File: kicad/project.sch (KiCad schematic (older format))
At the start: 33 parts, among them J1 Conn_01x05, J2 Conn_01x01, SW1 SW_DPDT_x2, U1 STM32L031F4Px

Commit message: Switches
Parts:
- removed SW1: SW_DPDT_x2, Buttons_Switches_THT:SW_Micro_SPST, symbol SW_DPDT_x2
- added R8: 1k, Resistors_SMD:R_0603_HandSoldering, symbol R
- added SW1: SW_SPDT, theapi:SW_Micro_SPST, symbol SW_SPDT
- added SW2: SW_SPDT, Buttons_Switches_THT:SW_Micro_SPST, symbol SW_SPDT
- added SW3: SW_Push, Buttons_Switches_THT:SW_PUSH_6mm, symbol SW_Push
- J2: footprint Mounting_Holes:MountingHole_2.5mm -> Mounting_Holes:MountingHole_2.5mm_Pad
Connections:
- net GND: now also R8.1
- net at U1.10 (PA4): now also SW3.1
- net +BATT renamed BATT_SW
- net BATT_SW: now also SW1.1 (A), SW2.1 (A)
- net BATT_UNSWITCHED renamed BATT+
- net BATT+: now also SW1.2 (B), SW2.2 (B)
- new net: R8.2, SW3.2
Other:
- note added: "Different sized switch\nfootprint options"
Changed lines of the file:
@@
 SWDIO
 $Comp
-L +BATT #PWR03
-U 1 1 5A9FF0BE
-P 5625 2325
-F 0 "#PWR03" H 5625 2175 50  0001 C CNN
-F 1 "+BATT" H 5625 2465 50  0000 C CNN
-F 2 "" H 5625 2325 50  0001 C CNN
-F 3 "" H 5625 2325 50  0001 C CNN
-	1    5625 2325
-	1    0    0    -1
-$EndComp
-$Comp
-L +BATT #PWR04
-U 1 1 5A9FF0BF
-P 2525 2825
-F 0 "#PWR04" H 2525 2675 50  0001 C CNN
-F 1 "+BATT" H 2525 2965 50  0000 C CNN
-F 2 "" H 2525 2825 50  0001 C CNN
-F 3 "" H 2525 2825 50  0001 C CNN
-	1    2525 2825
-	1    0    0    -1
-$EndComp
-$Comp
-L GND #PWR05
+L GND #PWR04
 U 1 1 5A9FF0C0
 P 2525 3750
-F 0 "#PWR05" H 2525 3500 50  0001 C CNN
+F 0 "#PWR04" H 2525 3500 50  0001 C CNN
 F 1 "GND" H 2525 3600 50  0000 C CNN
 F 2 "" H 2525 3750 50  0001 C CNN
@@
 $EndComp
 $Comp
-L +BATT #PWR06
-U 1 1 5A9FF0C2
-P 3025 975
-F 0 "#PWR06" H 3025 825 50  0001 C CNN
-F 1 "+BATT" H 3025 1115 50  0000 C CNN
-F 2 "" H 3025 975 50  0001 C CNN
-F 3 "" H 3025 975 50  0001 C CNN
-	1    3025 975
-	1    0    0    -1
-$EndComp
-$Comp
-L GND #PWR07
+L GND #PWR05
 U 1 1 5A9FF0C3
 P 1250 2000
-F 0 "#PWR07" H 1250 1750 50  0001 C CNN
+F 0 "#PWR05" H 1250 1750 50  0001 C CNN
 F 1 "GND" H 1250 1850 50  0000 C CNN
 F 2 "" H 1250 2000 50  0001 C CNN
@@
 $EndComp
 $Comp
-L GND #PWR08
+L GND #PWR06
 U 1 1 5A9FF0C6
 P 5050 2600
-F 0 "#PWR08" H 5050 2350 50  0001 C CNN
+F 0 "#PWR06" H 5050 2350 50  0001 C CNN
 F 1 "GND" H 5050 2450 50  0000 C CNN
 F 2 "" H 5050 2600 50  0001 C CNN
@@
 $EndComp
 $Comp
-L GND #PWR09
+L GND #PWR07
 U 1 1 5A9FF0C7
 P 6300 2600
-F 0 "#PWR09" H 6300 2350 50  0001 C CNN
+F 0 "#PWR07" H 6300 2350 50  0001 C CNN
 F 1 "GND" H 6300 2450 50  0000 C CNN
 F 2 "" H 6300 2600 50  0001 C CNN
@@
 $EndComp
 $Comp
-L GND #PWR010
+L GND #PWR08
 U 1 1 5A9FF286
 P 10275 2475
-F 0 "#PWR010" H 10275 2225 50  0001 C CNN
+F 0 "#PWR08" H 10275 2225 50  0001 C CNN
 F 1 "GND" H 10275 2325 50  0000 C CNN
 F 2 "" H 10275 2475 50  0001 C CNN
@@
 $EndComp
 $Comp
-L GND #PWR011
+L GND #PWR09
 U 1 1 5A9FF752
 P 10275 2850
-F 0 "#PWR011" H 10275 2600 50  0001 C CNN
+F 0 "#PWR09" H 10275 2600 50  0001 C CNN
 F 1 "GND" H 10275 2700 50  0000 C CNN
 F 2 "" H 10275 2850 50  0001 C CNN
@@
 $EndComp
 $Comp
-L GND #PWR012
+L GND #PWR010
 U 1 1 5A9FF7FA
 P 10275 3250
-F 0 "#PWR012" H 10275 3000 50  0001 C CNN
+F 0 "#PWR010" H 10275 3000 50  0001 C CNN
 F 1 "GND" H 10275 3100 50  0000 C CNN
 F 2 "" H 10275 3250 50  0001 C CNN
@@
 $EndComp
 $Comp
-L GND #PWR013
+L GND #PWR011
 U 1 1 5A9FF80C
 P 10275 3625
-F 0 "#PWR013" H 10275 3375 50  0001 C CNN
+F 0 "#PWR011" H 10275 3375 50  0001 C CNN
 F 1 "GND" H 10275 3475 50  0000 C CNN
 F 2 "" H 10275 3625 50  0001 C CNN
@@
 $EndComp
 $Comp
-L GND #PWR014
+L GND #PWR012
 U 1 1 5A9FFBFF
 P 10275 4000
-F 0 "#PWR014" H 10275 3750 50  0001 C CNN
+F 0 "#PWR012" H 10275 3750 50  0001 C CNN
 F 1 "GND" H 10275 3850 50  0000 C CNN
 F 2 "" H 10275 4000 50  0001 C CNN
@@
 $EndComp
 $Comp
-L GND #PWR015
+L GND #PWR013
 U 1 1 5A9FFC11
 P 10275 4375
-F 0 "#PWR015" H 10275 4125 50  0001 C CNN
+F 0 "#PWR013" H 10275 4125 50  0001 C CNN
 F 1 "GND" H 10275 4225 50  0000 C CNN
 F 2 "" H 10275 4375 50  0001 C CNN
@@
 $EndComp
 NoConn ~ 6175 4225
-NoConn ~ 6175 4325
 NoConn ~ 5175 4225
 NoConn ~ 5175 4325
-NoConn ~ 6175 3825
-Text Notes 3200 875  0    60   ~ 0
+Text Notes 3300 900  0    60   ~ 0
 3V
 Text Notes 675  825  0    60   ~ 12
@@
 Programming Header
 NoConn ~ 6175 3425
-$Comp
-L SW_DPDT_x2 SW1
-U 1 1 5AA401EC
-P 2050 1300
-F 0 "SW1" H 2050 1470 50  0000 C CNN
-F 1 "SW_DPDT_x2" H 2050 1100 50  0000 C CNN
-F 2 "Buttons_Switches_THT:SW_Micro_SPST" H 2050 1300 50  0001 C CNN
-F 3 "" H 2050 1300 50  0001 C CNN
-	1    2050 1300
-	1    0    0    -1
-$EndComp
-NoConn ~ 2250 1400
-$Comp
-L GND #PWR016
+NoConn ~ 2625 1200
+$Comp
+L GND #PWR014
 U 1 1 5AAE815A
 P 2275 5025
-F 0 "#PWR016" H 2275 4775 50  0001 C CNN
+F 0 "#PWR014" H 2275 4775 50  0001 C CNN
 F 1 "GND" H 2275 4875 50  0000 C CNN
 F 2 "" H 2275 5025 50  0001 C CNN
@@
 F 0 "J2" H 1975 4925 50  0000 C CNN
 F 1 "Conn_01x01" H 1975 4725 50  0000 C CNN
-F 2 "Mounting_Holes:MountingHole_2.5mm" H 1975 4825 50  0001 C CNN
+F 2 "Mounting_Holes:MountingHole_2.5mm_Pad" H 1975 4825 50  0001 C CNN
 F 3 "" H 1975 4825 50  0001 C CNN
 	1    1975 4825
@@
 Wire Wire Line
 	6300 2525 6300 2600
-Wire Wire Line
-	2250 1200 3025 1200
-Wire Wire Line
-	3025 1200 3025 975
 Wire Wire Line
 	2275 5025 2275 4825
@@
 	-1   0    0    -1
 $EndComp
-Text Label 1825 1300 2    60   ~ 0
-BATT_UNSWITCHED
+Text Label 1550 1300 2    60   ~ 0
+BATT+
+$Comp
+L R R8
+U 1 1 5AAEE015
+P 7575 4750
+F 0 "R8" V 7655 4750 50  0000 C CNN
+F 1 "1k" V 7575 4750 50  0000 C CNN
+F 2 "Resistors_SMD:R_0603_HandSoldering" V 7505 4750 50  0001 C CNN
+F 3 "" H 7575 4750 50  0001 C CNN
+	1    7575 4750
+	0    1    1    0
+$EndComp
+$Comp
+L GND #PWR015
+U 1 1 5AAEE0C4
+P 7800 4850
+F 0 "#PWR015" H 7800 4600 50  0001 C CNN
+F 1 "GND" H 7800 4700 50  0000 C CNN
+F 2 "" H 7800 4850 50  0001 C CNN
+F 3 "" H 7800 4850 50  0001 C CNN
+	1    7800 4850
+	1    0    0    -1
+$EndComp
+Wire Wire Line
+	7800 4850 7800 4750
+Wire Wire Line
+	7800 4750 7725 4750
+Wire Wire Line
+	7025 3825 7025 4750
+$Comp
+L SW_SPDT SW1
+U 1 1 5AAEE9A7
+P 2425 1100
+F 0 "SW1" H 2425 1270 50  0000 C CNN
+F 1 "SW_SPDT" H 2425 900 50  0000 C CNN
+F 2 "theapi:SW_Micro_SPST" H 2425 1100 50  0001 C CNN
+F 3 "" H 2425 1100 50  0001 C CNN
+	1    2425 1100
+	1    0    0    -1
+$EndComp
+$Comp
+L SW_SPDT SW2
+U 1 1 5AAEEB45
+P 2425 1650
+F 0 "SW2" H 2425 1820 50  0000 C CNN
+F 1 "SW_SPDT" H 2425 1450 50  0000 C CNN
+F 2 "Buttons_Switches_THT:SW_Micro_SPST" H 2425 1650 50  0001 C CNN
+F 3 "" H 2425 1650 50  0001 C CNN
+	1    2425 1650
+	1    0    0    -1
+$EndComp
+Text GLabel 3125 1000 2    60   Input ~ 0
+BATT_SW
+Wire Wire Line
+	2225 1100 1850 1100
+Wire Wire Line
+	1850 1100 1850 1650
+Wire Wire Line
+	1850 1650 2225 1650
+Connection ~ 1850 1300
+Wire Wire Line
+	2625 1000 3125 1000
+Wire Wire Line
+	2625 1550 2900 1550
+Wire Wire Line
+	2900 1550 2900 1000
+Connection ~ 2900 1000
+NoConn ~ 2625 1750
+Text Notes 1525 950  0    60   ~ 0
+Different sized switch\nfootprint options
+Text GLabel 5625 2000 0    60   Input ~ 0
+BATT_SW
+Wire Wire Line
+	5625 2325 5625 2000
+$Comp
+L SW_Push SW3
+U 1 1 5AAEFB1B
+P 7225 4750
+F 0 "SW3" H 7275 4850 50  0000 L CNN
+F 1 "SW_Push" H 7225 4690 50  0000 C CNN
+F 2 "Buttons_Switches_THT:SW_PUSH_6mm" H 7225 4950 50  0001 C CNN
+F 3 "" H 7225 4950 50  0001 C CNN
+	1    7225 4750
+	1    0    0    -1
+$EndComp
+Wire Wire Line
+	6175 3825 7025 3825
+NoConn ~ 6175 4325
+Text GLabel 2525 2825 2    60   Input ~ 0
+BATT_SW
 $EndSCHEMATC

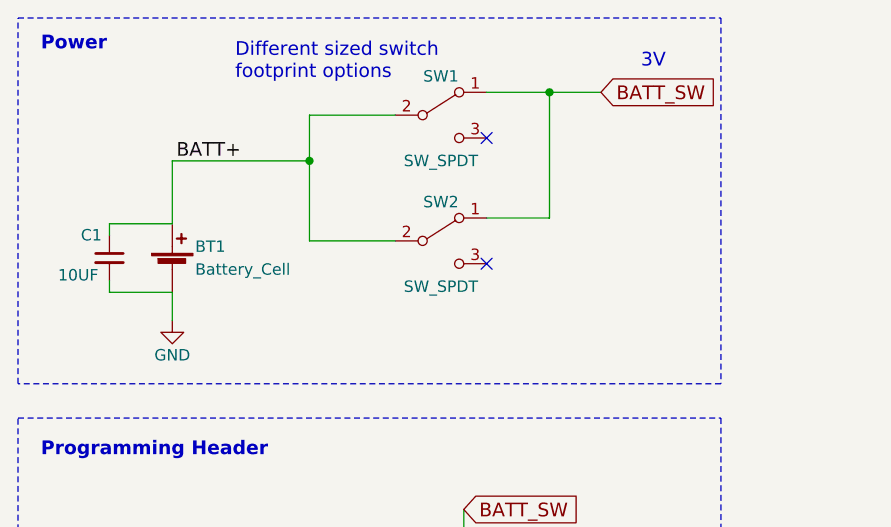
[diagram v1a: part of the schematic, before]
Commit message: Reverse polarity protection
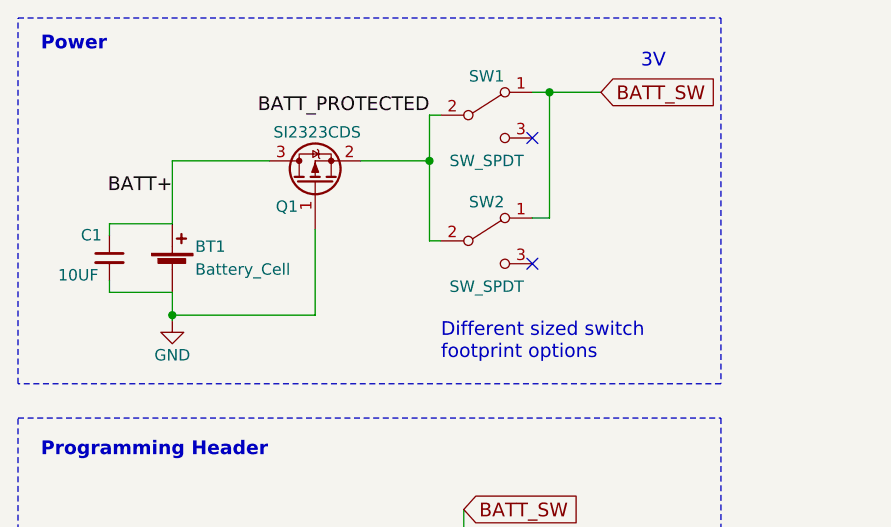
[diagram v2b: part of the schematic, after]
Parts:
- added Q1: SI2323CDS, TO_SOT_Packages_SMD:SOT-23_Handsoldering, symbol Q_PMOS_GSD
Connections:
- net BATT+: now also Q1.3 (D); no longer SW1.2 (B), SW2.2 (B)
- net GND: now also Q1.1 (G)
- new net BATT_PROTECTED: Q1.2 (S), SW1.2 (B), SW2.2 (B)
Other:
- moved on the sheet: SW1, SW2
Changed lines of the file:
@@
 SWDIO
 $Comp
-L GND #PWR04
+L GND #PWR03
 U 1 1 5A9FF0C0
 P 2525 3750
-F 0 "#PWR04" H 2525 3500 50  0001 C CNN
+F 0 "#PWR03" H 2525 3500 50  0001 C CNN
 F 1 "GND" H 2525 3600 50  0000 C CNN
 F 2 "" H 2525 3750 50  0001 C CNN
@@
 $EndComp
 $Comp
-L GND #PWR05
+L GND #PWR04
 U 1 1 5A9FF0C3
 P 1250 2000
-F 0 "#PWR05" H 1250 1750 50  0001 C CNN
+F 0 "#PWR04" H 1250 1750 50  0001 C CNN
 F 1 "GND" H 1250 1850 50  0000 C CNN
 F 2 "" H 1250 2000 50  0001 C CNN
@@
 $EndComp
 $Comp
-L GND #PWR06
+L GND #PWR05
 U 1 1 5A9FF0C6
 P 5050 2600
-F 0 "#PWR06" H 5050 2350 50  0001 C CNN
+F 0 "#PWR05" H 5050 2350 50  0001 C CNN
 F 1 "GND" H 5050 2450 50  0000 C CNN
 F 2 "" H 5050 2600 50  0001 C CNN
@@
 $EndComp
 $Comp
-L GND #PWR07
+L GND #PWR06
 U 1 1 5A9FF0C7
 P 6300 2600
-F 0 "#PWR07" H 6300 2350 50  0001 C CNN
+F 0 "#PWR06" H 6300 2350 50  0001 C CNN
 F 1 "GND" H 6300 2450 50  0000 C CNN
 F 2 "" H 6300 2600 50  0001 C CNN
@@
 $EndComp
 $Comp
-L GND #PWR08
+L GND #PWR07
 U 1 1 5A9FF286
 P 10275 2475
-F 0 "#PWR08" H 10275 2225 50  0001 C CNN
+F 0 "#PWR07" H 10275 2225 50  0001 C CNN
 F 1 "GND" H 10275 2325 50  0000 C CNN
 F 2 "" H 10275 2475 50  0001 C CNN
@@
 $EndComp
 $Comp
-L GND #PWR09
+L GND #PWR08
 U 1 1 5A9FF752
 P 10275 2850
-F 0 "#PWR09" H 10275 2600 50  0001 C CNN
+F 0 "#PWR08" H 10275 2600 50  0001 C CNN
 F 1 "GND" H 10275 2700 50  0000 C CNN
 F 2 "" H 10275 2850 50  0001 C CNN
@@
 $EndComp
 $Comp
-L GND #PWR010
+L GND #PWR09
 U 1 1 5A9FF7FA
 P 10275 3250
-F 0 "#PWR010" H 10275 3000 50  0001 C CNN
+F 0 "#PWR09" H 10275 3000 50  0001 C CNN
 F 1 "GND" H 10275 3100 50  0000 C CNN
 F 2 "" H 10275 3250 50  0001 C CNN
@@
 $EndComp
 $Comp
-L GND #PWR011
+L GND #PWR010
 U 1 1 5A9FF80C
 P 10275 3625
-F 0 "#PWR011" H 10275 3375 50  0001 C CNN
+F 0 "#PWR010" H 10275 3375 50  0001 C CNN
 F 1 "GND" H 10275 3475 50  0000 C CNN
 F 2 "" H 10275 3625 50  0001 C CNN
@@
 $EndComp
 $Comp
-L GND #PWR012
+L GND #PWR011
 U 1 1 5A9FFBFF
 P 10275 4000
-F 0 "#PWR012" H 10275 3750 50  0001 C CNN
+F 0 "#PWR011" H 10275 3750 50  0001 C CNN
 F 1 "GND" H 10275 3850 50  0000 C CNN
 F 2 "" H 10275 4000 50  0001 C CNN
@@
 $EndComp
 $Comp
-L GND #PWR013
+L GND #PWR012
 U 1 1 5A9FFC11
 P 10275 4375
-F 0 "#PWR013" H 10275 4125 50  0001 C CNN
+F 0 "#PWR012" H 10275 4125 50  0001 C CNN
 F 1 "GND" H 10275 4225 50  0000 C CNN
 F 2 "" H 10275 4375 50  0001 C CNN
@@
 Programming Header
 NoConn ~ 6175 3425
-NoConn ~ 2625 1200
-$Comp
-L GND #PWR014
+NoConn ~ 2825 1200
+$Comp
+L GND #PWR013
 U 1 1 5AAE815A
 P 2275 5025
-F 0 "#PWR014" H 2275 4775 50  0001 C CNN
+F 0 "#PWR013" H 2275 4775 50  0001 C CNN
 F 1 "GND" H 2275 4875 50  0000 C CNN
 F 2 "" H 2275 5025 50  0001 C CNN
@@
 	575  2275 575  675
 Wire Wire Line
-	1250 1300 1850 1300
-Wire Wire Line
-	1250 2000 1250 1875
+	1250 1875 1250 2000
 Wire Notes Line
 	575  2425 3650 2425
@@
 	-1   0    0    -1
 $EndComp
-Text Label 1550 1300 2    60   ~ 0
+Text Label 1250 1450 2    60   ~ 0
 BATT+
 $Comp
@@
 $EndComp
 $Comp
-L GND #PWR015
+L GND #PWR014
 U 1 1 5AAEE0C4
 P 7800 4850
-F 0 "#PWR015" H 7800 4600 50  0001 C CNN
+F 0 "#PWR014" H 7800 4600 50  0001 C CNN
 F 1 "GND" H 7800 4700 50  0000 C CNN
 F 2 "" H 7800 4850 50  0001 C CNN
@@
 L SW_SPDT SW1
 U 1 1 5AAEE9A7
-P 2425 1100
-F 0 "SW1" H 2425 1270 50  0000 C CNN
-F 1 "SW_SPDT" H 2425 900 50  0000 C CNN
-F 2 "theapi:SW_Micro_SPST" H 2425 1100 50  0001 C CNN
-F 3 "" H 2425 1100 50  0001 C CNN
-	1    2425 1100
+P 2625 1100
+F 0 "SW1" H 2625 1270 50  0000 C CNN
+F 1 "SW_SPDT" H 2625 900 50  0000 C CNN
+F 2 "theapi:SW_Micro_SPST" H 2625 1100 50  0001 C CNN
+F 3 "" H 2625 1100 50  0001 C CNN
+	1    2625 1100
 	1    0    0    -1
 $EndComp
@@
 L SW_SPDT SW2
 U 1 1 5AAEEB45
-P 2425 1650
-F 0 "SW2" H 2425 1820 50  0000 C CNN
-F 1 "SW_SPDT" H 2425 1450 50  0000 C CNN
-F 2 "Buttons_Switches_THT:SW_Micro_SPST" H 2425 1650 50  0001 C CNN
-F 3 "" H 2425 1650 50  0001 C CNN
-	1    2425 1650
+P 2625 1650
+F 0 "SW2" H 2625 1820 50  0000 C CNN
+F 1 "SW_SPDT" H 2625 1450 50  0000 C CNN
+F 2 "Buttons_Switches_THT:SW_Micro_SPST" H 2625 1650 50  0001 C CNN
+F 3 "" H 2625 1650 50  0001 C CNN
+	1    2625 1650
 	1    0    0    -1
 $EndComp
@@
 BATT_SW
 Wire Wire Line
-	2225 1100 1850 1100
-Wire Wire Line
-	1850 1100 1850 1650
-Wire Wire Line
-	1850 1650 2225 1650
-Connection ~ 1850 1300
-Wire Wire Line
-	2625 1000 3125 1000
-Wire Wire Line
-	2625 1550 2900 1550
+	2425 1100 2375 1100
+Wire Wire Line
+	2375 1100 2375 1650
+Wire Wire Line
+	2375 1650 2425 1650
+Connection ~ 2375 1300
+Wire Wire Line
+	2825 1000 3125 1000
+Wire Wire Line
+	2825 1550 2900 1550
 Wire Wire Line
 	2900 1550 2900 1000
 Connection ~ 2900 1000
-NoConn ~ 2625 1750
-Text Notes 1525 950  0    60   ~ 0
+NoConn ~ 2825 1750
+Text Notes 2425 2175 0    60   ~ 0
 Different sized switch\nfootprint options
 Text GLabel 5625 2000 0    60   Input ~ 0
@@
 Text GLabel 2525 2825 2    60   Input ~ 0
 BATT_SW
+Wire Wire Line
+	1250 1300 1675 1300
+Wire Wire Line
+	2075 1300 2375 1300
+Wire Wire Line
+	1875 1975 1250 1975
+Connection ~ 1250 1975
+$Comp
+L Q_PMOS_GSD Q1
+U 1 1 5AB0C500
+P 1875 1400
+F 0 "Q1" V 1775 1475 50  0000 L CNN
+F 1 "SI2323CDS" V 2100 1200 50  0000 L CNN
+F 2 "TO_SOT_Packages_SMD:SOT-23_Handsoldering" H 2075 1500 50  0001 C CNN
+F 3 "" H 1875 1400 50  0001 C CNN
+	1    1875 1400
+	0    -1   -1   0
+$EndComp
+Wire Wire Line
+	1875 1600 1875 1975
+Text Label 2375 1100 2    60   ~ 0
+BATT_PROTECTED
 $EndSCHEMATC

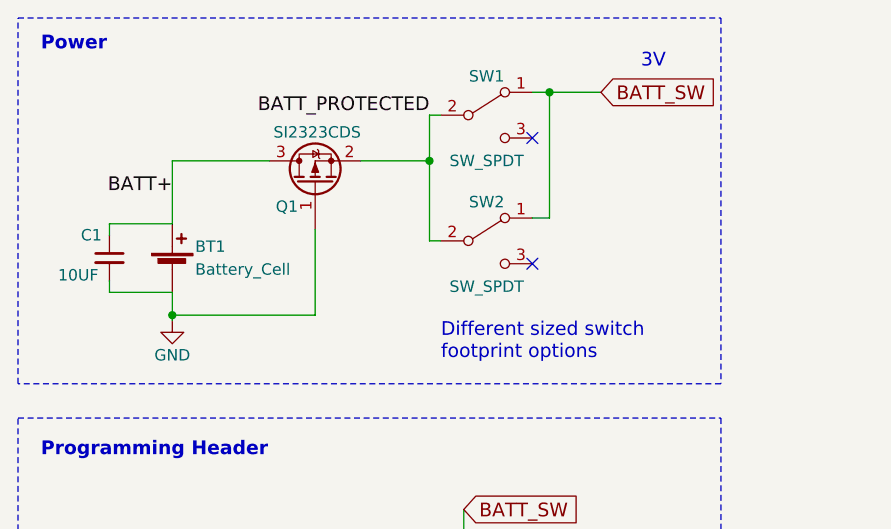
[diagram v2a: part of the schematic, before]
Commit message: Cap after switch
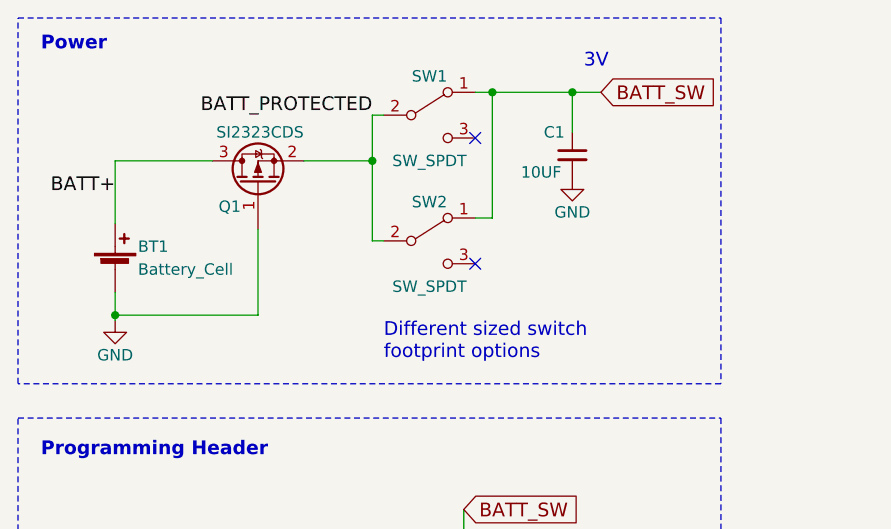
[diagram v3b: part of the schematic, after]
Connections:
- net BATT+: no longer C1.1
- net BATT_SW: now also C1.1
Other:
- moved on the sheet: BT1, C1, Q1, SW1, SW2
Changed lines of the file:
@@
 L Battery_Cell BT1
 U 1 1 5A9FF0C1
-P 1250 1775
-F 0 "BT1" H 1350 1875 50  0000 L CNN
-F 1 "Battery_Cell" H 1350 1775 50  0000 L CNN
-F 2 "theapi:CR2032H" V 1250 1835 50  0001 C CNN
-F 3 "" V 1250 1835 50  0001 C CNN
-	1    1250 1775
+P 1000 1775
+F 0 "BT1" H 1100 1875 50  0000 L CNN
+F 1 "Battery_Cell" H 1100 1775 50  0000 L CNN
+F 2 "theapi:CR2032H" V 1000 1835 50  0001 C CNN
+F 3 "" V 1000 1835 50  0001 C CNN
+	1    1000 1775
 	1    0    0    -1
 $EndComp
@@
 L GND #PWR04
 U 1 1 5A9FF0C3
-P 1250 2000
-F 0 "#PWR04" H 1250 1750 50  0001 C CNN
-F 1 "GND" H 1250 1850 50  0000 C CNN
-F 2 "" H 1250 2000 50  0001 C CNN
-F 3 "" H 1250 2000 50  0001 C CNN
-	1    1250 2000
+P 1000 2000
+F 0 "#PWR04" H 1000 1750 50  0001 C CNN
+F 1 "GND" H 1000 1850 50  0000 C CNN
+F 2 "" H 1000 2000 50  0001 C CNN
+F 3 "" H 1000 2000 50  0001 C CNN
+	1    1000 2000
 	1    0    0    -1
 $EndComp
@@
 L C_Small C1
 U 1 1 5A9FF0C8
-P 975 1725
-F 0 "C1" H 850 1825 50  0000 L CNN
-F 1 "10UF" H 750 1650 50  0000 L CNN
-F 2 "Capacitors_SMD:C_0805_HandSoldering" H 975 1725 50  0001 C CNN
-F 3 "" H 975 1725 50  0001 C CNN
-	1    975  1725
+P 3000 1275
+F 0 "C1" H 2875 1375 50  0000 L CNN
+F 1 "10UF" H 2775 1200 50  0000 L CNN
+F 2 "Capacitors_SMD:C_0805_HandSoldering" H 3000 1275 50  0001 C CNN
+F 3 "" H 3000 1275 50  0001 C CNN
+	1    3000 1275
 	1    0    0    -1
 $EndComp
@@
 NoConn ~ 5175 4225
 NoConn ~ 5175 4325
-Text Notes 3300 900  0    60   ~ 0
+Text Notes 3050 900  0    60   ~ 0
 3V
 Text Notes 675  825  0    60   ~ 12
@@
 Programming Header
 NoConn ~ 6175 3425
-NoConn ~ 2825 1200
+NoConn ~ 2575 1200
 $Comp
 L GND #PWR013
@@
 Connection ~ 5575 2525
 Wire Wire Line
-	1250 1575 975  1575
-Wire Wire Line
-	975  1575 975  1625
-Wire Wire Line
-	1250 1875 975  1875
-Wire Wire Line
-	975  1875 975  1825
-Wire Wire Line
 	6175 3525 6775 3525
 Wire Wire Line
@@
 	7375 4075 7475 4075
 Wire Wire Line
-	1250 1300 1250 1575
+	1000 1300 1000 1575
 Wire Notes Line
 	575  675  3650 675
@@
 	575  2275 575  675
 Wire Wire Line
-	1250 1875 1250 2000
+	1000 1875 1000 2000
 Wire Notes Line
 	575  2425 3650 2425
@@
 	-1   0    0    -1
 $EndComp
-Text Label 1250 1450 2    60   ~ 0
+Text Label 1000 1450 2    60   ~ 0
 BATT+
 $Comp
@@
 L SW_SPDT SW1
 U 1 1 5AAEE9A7
-P 2625 1100
-F 0 "SW1" H 2625 1270 50  0000 C CNN
-F 1 "SW_SPDT" H 2625 900 50  0000 C CNN
-F 2 "theapi:SW_Micro_SPST" H 2625 1100 50  0001 C CNN
-F 3 "" H 2625 1100 50  0001 C CNN
-	1    2625 1100
+P 2375 1100
+F 0 "SW1" H 2375 1270 50  0000 C CNN
+F 1 "SW_SPDT" H 2375 900 50  0000 C CNN
+F 2 "theapi:SW_Micro_SPST" H 2375 1100 50  0001 C CNN
+F 3 "" H 2375 1100 50  0001 C CNN
+	1    2375 1100
 	1    0    0    -1
 $EndComp
@@
 L SW_SPDT SW2
 U 1 1 5AAEEB45
-P 2625 1650
-F 0 "SW2" H 2625 1820 50  0000 C CNN
-F 1 "SW_SPDT" H 2625 1450 50  0000 C CNN
-F 2 "Buttons_Switches_THT:SW_Micro_SPST" H 2625 1650 50  0001 C CNN
-F 3 "" H 2625 1650 50  0001 C CNN
-	1    2625 1650
+P 2375 1650
+F 0 "SW2" H 2375 1820 50  0000 C CNN
+F 1 "SW_SPDT" H 2375 1450 50  0000 C CNN
+F 2 "Buttons_Switches_THT:SW_Micro_SPST" H 2375 1650 50  0001 C CNN
+F 3 "" H 2375 1650 50  0001 C CNN
+	1    2375 1650
 	1    0    0    -1
 $EndComp
@@
 BATT_SW
 Wire Wire Line
-	2425 1100 2375 1100
-Wire Wire Line
-	2375 1100 2375 1650
-Wire Wire Line
-	2375 1650 2425 1650
-Connection ~ 2375 1300
-Wire Wire Line
-	2825 1000 3125 1000
-Wire Wire Line
-	2825 1550 2900 1550
-Wire Wire Line
-	2900 1550 2900 1000
-Connection ~ 2900 1000
-NoConn ~ 2825 1750
-Text Notes 2425 2175 0    60   ~ 0
+	2175 1100 2125 1100
+Wire Wire Line
+	2125 1100 2125 1650
+Wire Wire Line
+	2125 1650 2175 1650
+Connection ~ 2125 1300
+Wire Wire Line
+	2575 1000 3125 1000
+Wire Wire Line
+	2575 1550 2650 1550
+Wire Wire Line
+	2650 1550 2650 1000
+Connection ~ 2650 1000
+NoConn ~ 2575 1750
+Text Notes 2175 2175 0    60   ~ 0
 Different sized switch\nfootprint options
 Text GLabel 5625 2000 0    60   Input ~ 0
@@
 BATT_SW
 Wire Wire Line
-	1250 1300 1675 1300
-Wire Wire Line
-	2075 1300 2375 1300
-Wire Wire Line
-	1875 1975 1250 1975
-Connection ~ 1250 1975
+	1000 1300 1425 1300
+Wire Wire Line
+	1825 1300 2125 1300
+Wire Wire Line
+	1625 1975 1000 1975
+Connection ~ 1000 1975
 $Comp
 L Q_PMOS_GSD Q1
 U 1 1 5AB0C500
-P 1875 1400
-F 0 "Q1" V 1775 1475 50  0000 L CNN
-F 1 "SI2323CDS" V 2100 1200 50  0000 L CNN
-F 2 "TO_SOT_Packages_SMD:SOT-23_Handsoldering" H 2075 1500 50  0001 C CNN
-F 3 "" H 1875 1400 50  0001 C CNN
-	1    1875 1400
-	0    -1   -1   0
-$EndComp
-Wire Wire Line
-	1875 1600 1875 1975
-Text Label 2375 1100 2    60   ~ 0
+P 1625 1400
+F 0 "Q1" V 1525 1475 50  0000 L CNN
+F 1 "SI2323CDS" V 1850 1200 50  0000 L CNN
+F 2 "TO_SOT_Packages_SMD:SOT-23_Handsoldering" H 1825 1500 50  0001 C CNN
+F 3 "" H 1625 1400 50  0001 C CNN
+	1    1625 1400
+	0    -1   -1   0
+$EndComp
+Wire Wire Line
+	1625 1600 1625 1975
+Text Label 2125 1100 2    60   ~ 0
 BATT_PROTECTED
+Wire Wire Line
+	3000 1175 3000 1000
+Connection ~ 3000 1000
+$Comp
+L GND #PWR015
+U 1 1 5AB0E7F5
+P 3000 1375
+F 0 "#PWR015" H 3000 1125 50  0001 C CNN
+F 1 "GND" H 3000 1225 50  0000 C CNN
+F 2 "" H 3000 1375 50  0001 C CNN
+F 3 "" H 3000 1375 50  0001 C CNN
+	1    3000 1375
+	1    0    0    -1
+$EndComp
 $EndSCHEMATC

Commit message: Labels
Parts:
- J1: footprint Pin_Headers:Pin_Header_Straight_1x05_Pitch2.54mm -> theapi:SWD_Header
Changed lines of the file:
@@
 F 0 "J1" H 1850 3575 50  0000 C CNN
 F 1 "Conn_01x05" H 1850 2975 50  0000 C CNN
-F 2 "Pin_Headers:Pin_Header_Straight_1x05_Pitch2.54mm" H 1850 3275 50  0001 C CNN
+F 2 "theapi:SWD_Header" H 1850 3275 50  0001 C CNN
 F 3 "" H 1850 3275 50  0001 C CNN
 	1    1850 3275
